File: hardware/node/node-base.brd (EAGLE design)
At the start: 100 x 80 mm, 57 parts, among them IC1 HYPERTRIANGLE_TCS3472FN, Q1 32.768kHz, Q2 24MHz, Q3 BS250, U1 INA322_DGK_8, U2 LMV551_DBV_5, X1 BU-SMA-V

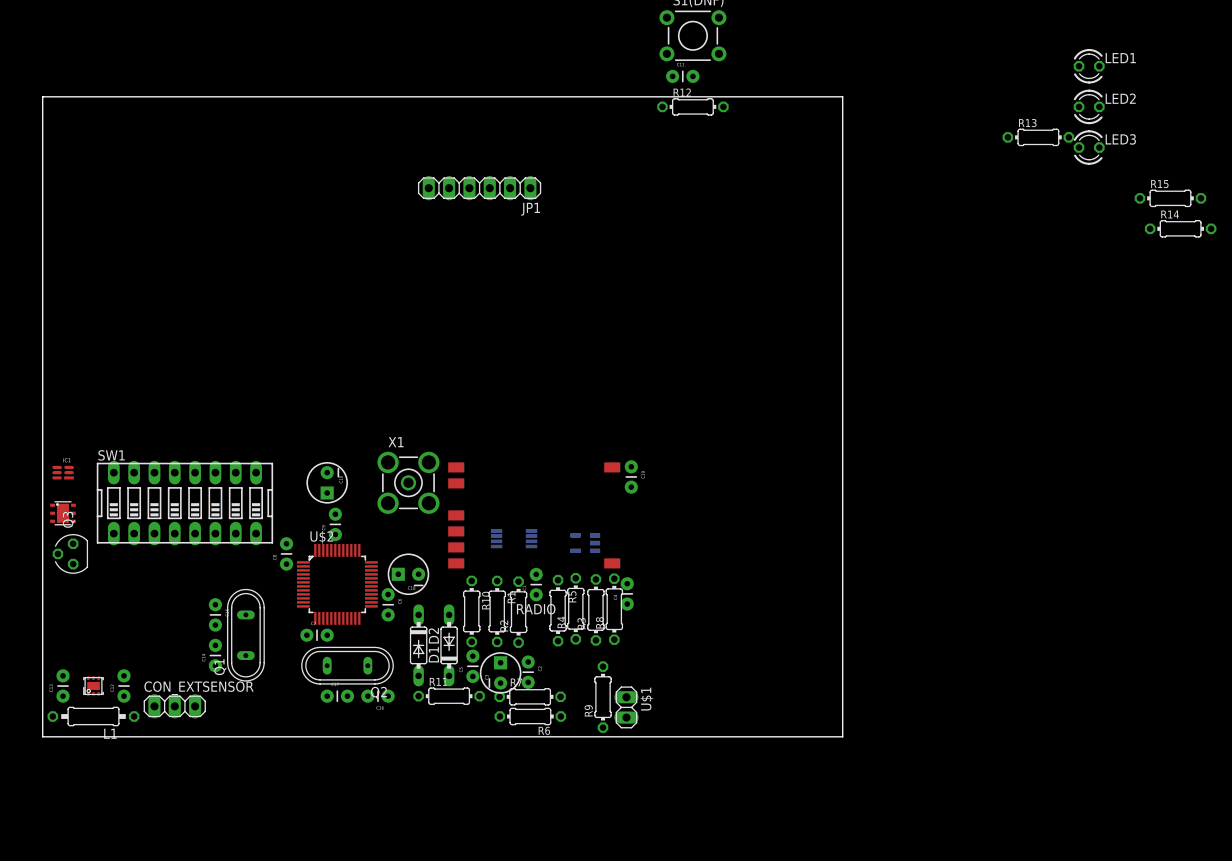
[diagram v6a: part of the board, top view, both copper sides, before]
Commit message: NODEHW: Routeing starts
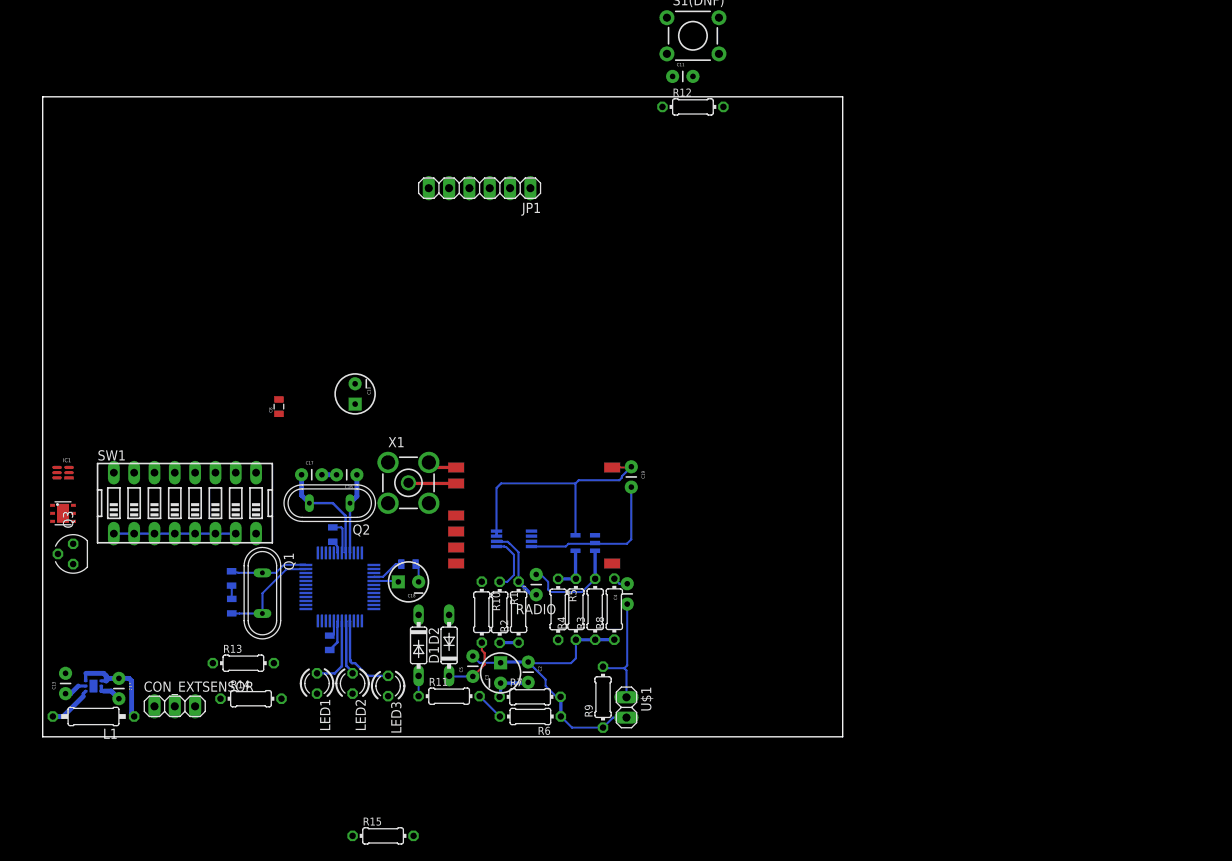
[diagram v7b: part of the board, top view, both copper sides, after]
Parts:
- C14, C15, C6, C7, C8, C9: device SparkFun-Capacitors:CAP-PTH-SMALL -> SparkFun-Capacitors:0805
- moved R14 130.2 mm to (26.0, 4.76)
- moved R15 126.6 mm to (42.5, -12.4)
- moved LED1 123.6 mm to (34.3, 6.67), turned to 270 degrees
- moved R13 119.1 mm to (25.1, 9.21)
- moved LED2 116.9 mm to (38.7, 6.67), turned to 270 degrees
- moved LED3 110.5 mm to (43.2, 6.35), turned to 270 degrees
- moved C16 27.9 mm to (39.3, 32.8)
- moved C17 27.9 mm to (32.4, 32.8)
- moved Q2 20.4 mm to (35.9, 29.2)
- moved C8 19.7 mm to (29.5, 41.3)
- moved C10 11.6 mm to (39.1, 42.9)
- moved C14 11.1 mm to (23.6, 19.8), flipped to the bottom, turned to 270 degrees
- moved Q1 5.65 mm to (27.5, 18.0), turned to 270 degrees
- moved C6 4.58 mm to (45.7, 21.6), flipped to the bottom, turned to 180 degrees
- moved C7 3.01 mm to (35.9, 11.7), flipped to the bottom, turned to 90 degrees
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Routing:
- net GND: track 0.00 -> 56.7 mm
- net +3V3: track 0.00 -> 52.6 mm
- net VCC/2: track 0.00 -> 38.5 mm
- net PIEZO_OUT: track 0.00 -> 14.9 mm
- net XTALN: track 0.00 -> 13.8 mm
- net LFXTAL_N: track 0.00 -> 13.1 mm
- net INSTR_FILTERED: track 0.00 -> 13.0 mm
- net V+: track 0.00 -> 12.9 mm
- net LED_GREEN: track 0.00 -> 10.6 mm
- net XTALP: track 0.00 -> 10.1 mm
- net INSTR_OUT: track 0.00 -> 9.92 mm
- net LFXTAL_P: track 0.00 -> 9.75 mm
- net LED_RED: track 0.00 -> 9.13 mm
- net DETECT_OUT: track 0.00 -> 7.98 mm
- net REFLINE: track 0.00 -> 7.28 mm
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
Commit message: NODEHW: Routeing ongoing
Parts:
- CON_EXTSENSOR: device pinhead:1X03 -> pinhead:1X04
- moved CON_EXTSENSOR 55.0 mm to (58.7, 39.1)
- moved SW1 1.31 mm to (18.1, 30.5), turned to 180 degrees
- renumbered JP1 to DEBUG
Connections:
- net +3V3: now also CON_EXTSENSOR.1
- net EXTSENS_RX: now also CON_EXTSENSOR.3; no longer CON_EXTSENSOR.2
- net EXTSENS_TX: now also CON_EXTSENSOR.2; no longer CON_EXTSENSOR.1
- net GND: now also CON_EXTSENSOR.4; no longer CON_EXTSENSOR.3
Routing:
- net OPAMP_OUT: track 0.00 -> 44.4 mm, vias 0 -> 1
- net +3V3: track 52.6 -> 73.4 mm
- net GND: track 56.7 -> 64.9 mm, vias 0 -> 1
- net REFLINE: track 7.28 -> 0.00 mm
- net INSTR_OUT: track 9.92 -> 3.66 mm
